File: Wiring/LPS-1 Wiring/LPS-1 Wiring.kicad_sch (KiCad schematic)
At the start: 9 parts, among them J1 Block_Connector_04_b, J2 Battery, J3 Solar charging unit, J4 Solar Panel, J5 LPS-1 Monitoring Unit, J6 Fuse Block, J7 Block_Connector_04_b, SW1 Battery Kill Switch, SW2 Load Monitoring Control

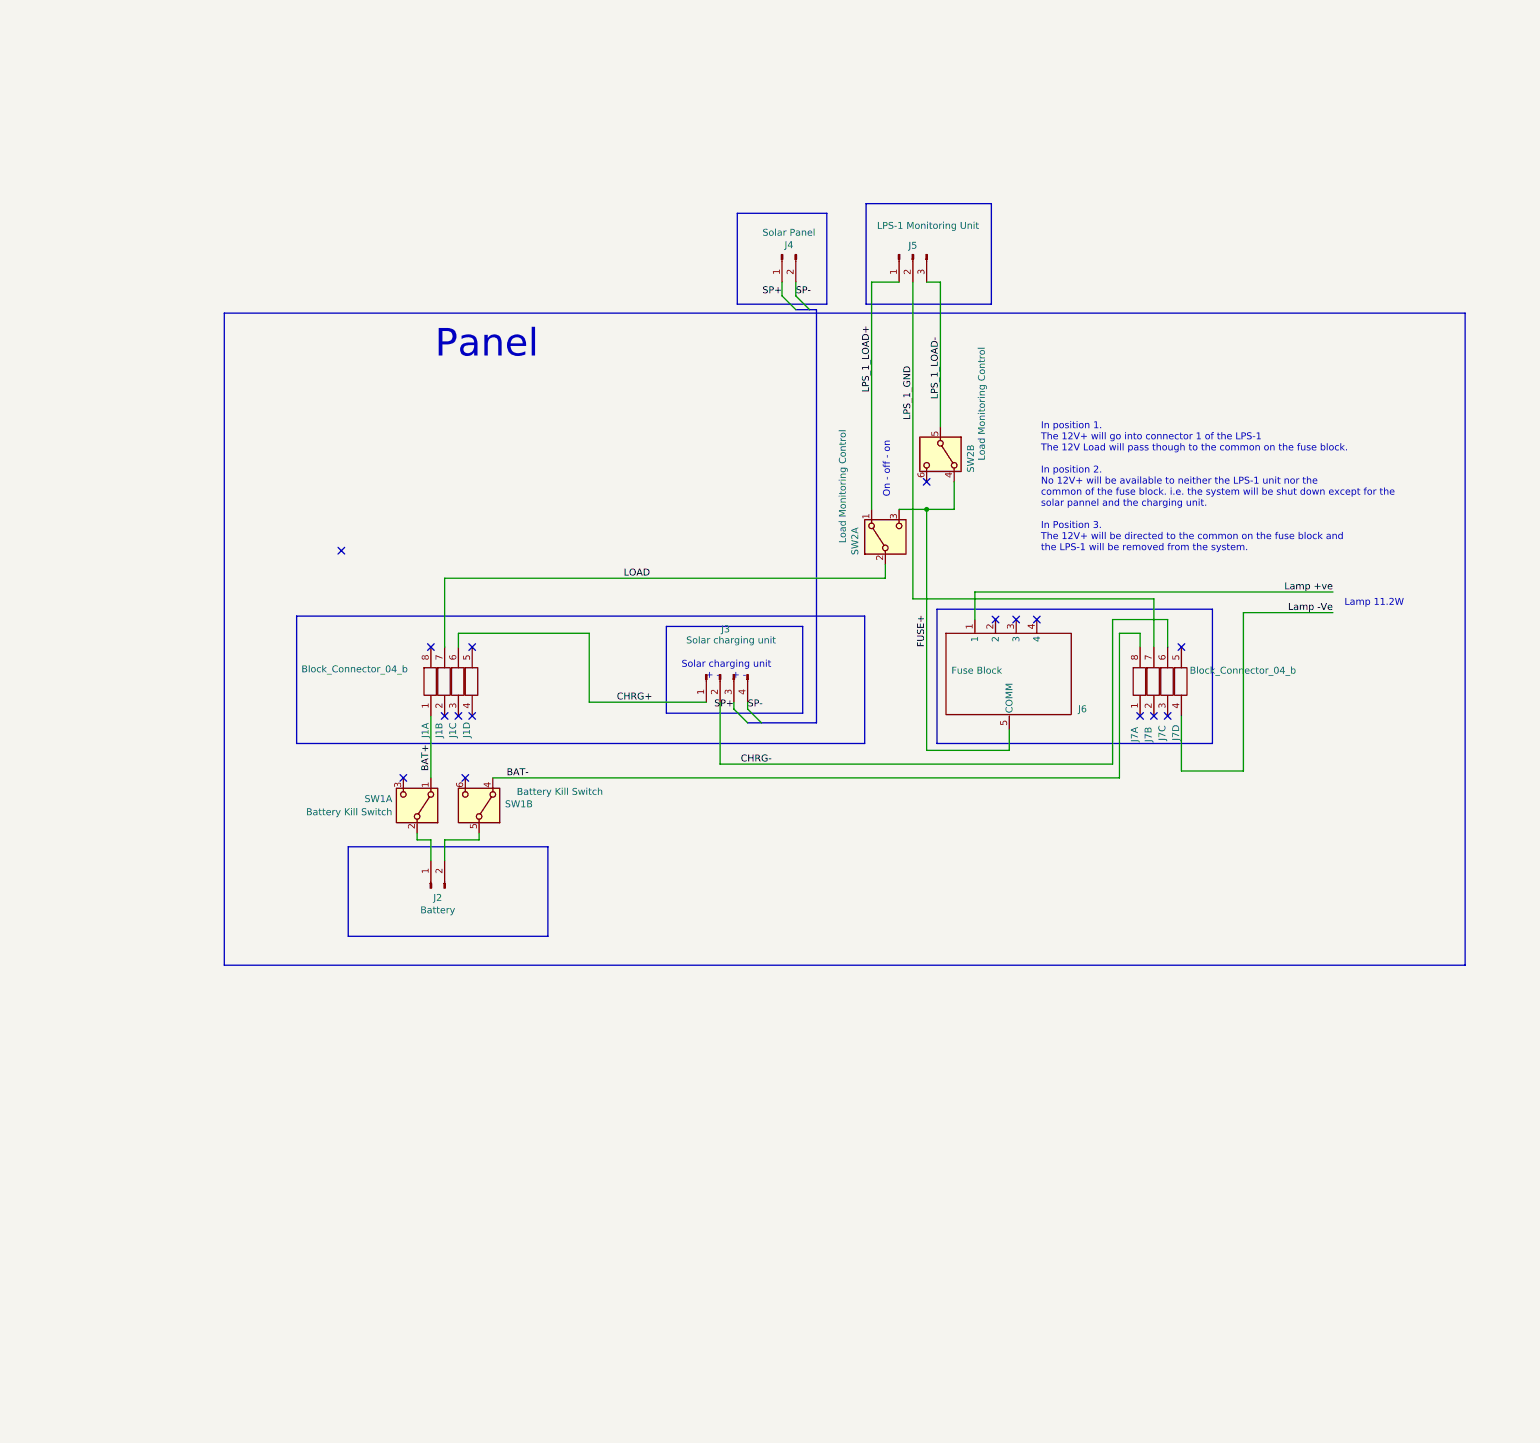
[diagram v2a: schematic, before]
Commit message: Updated the wiring diagram
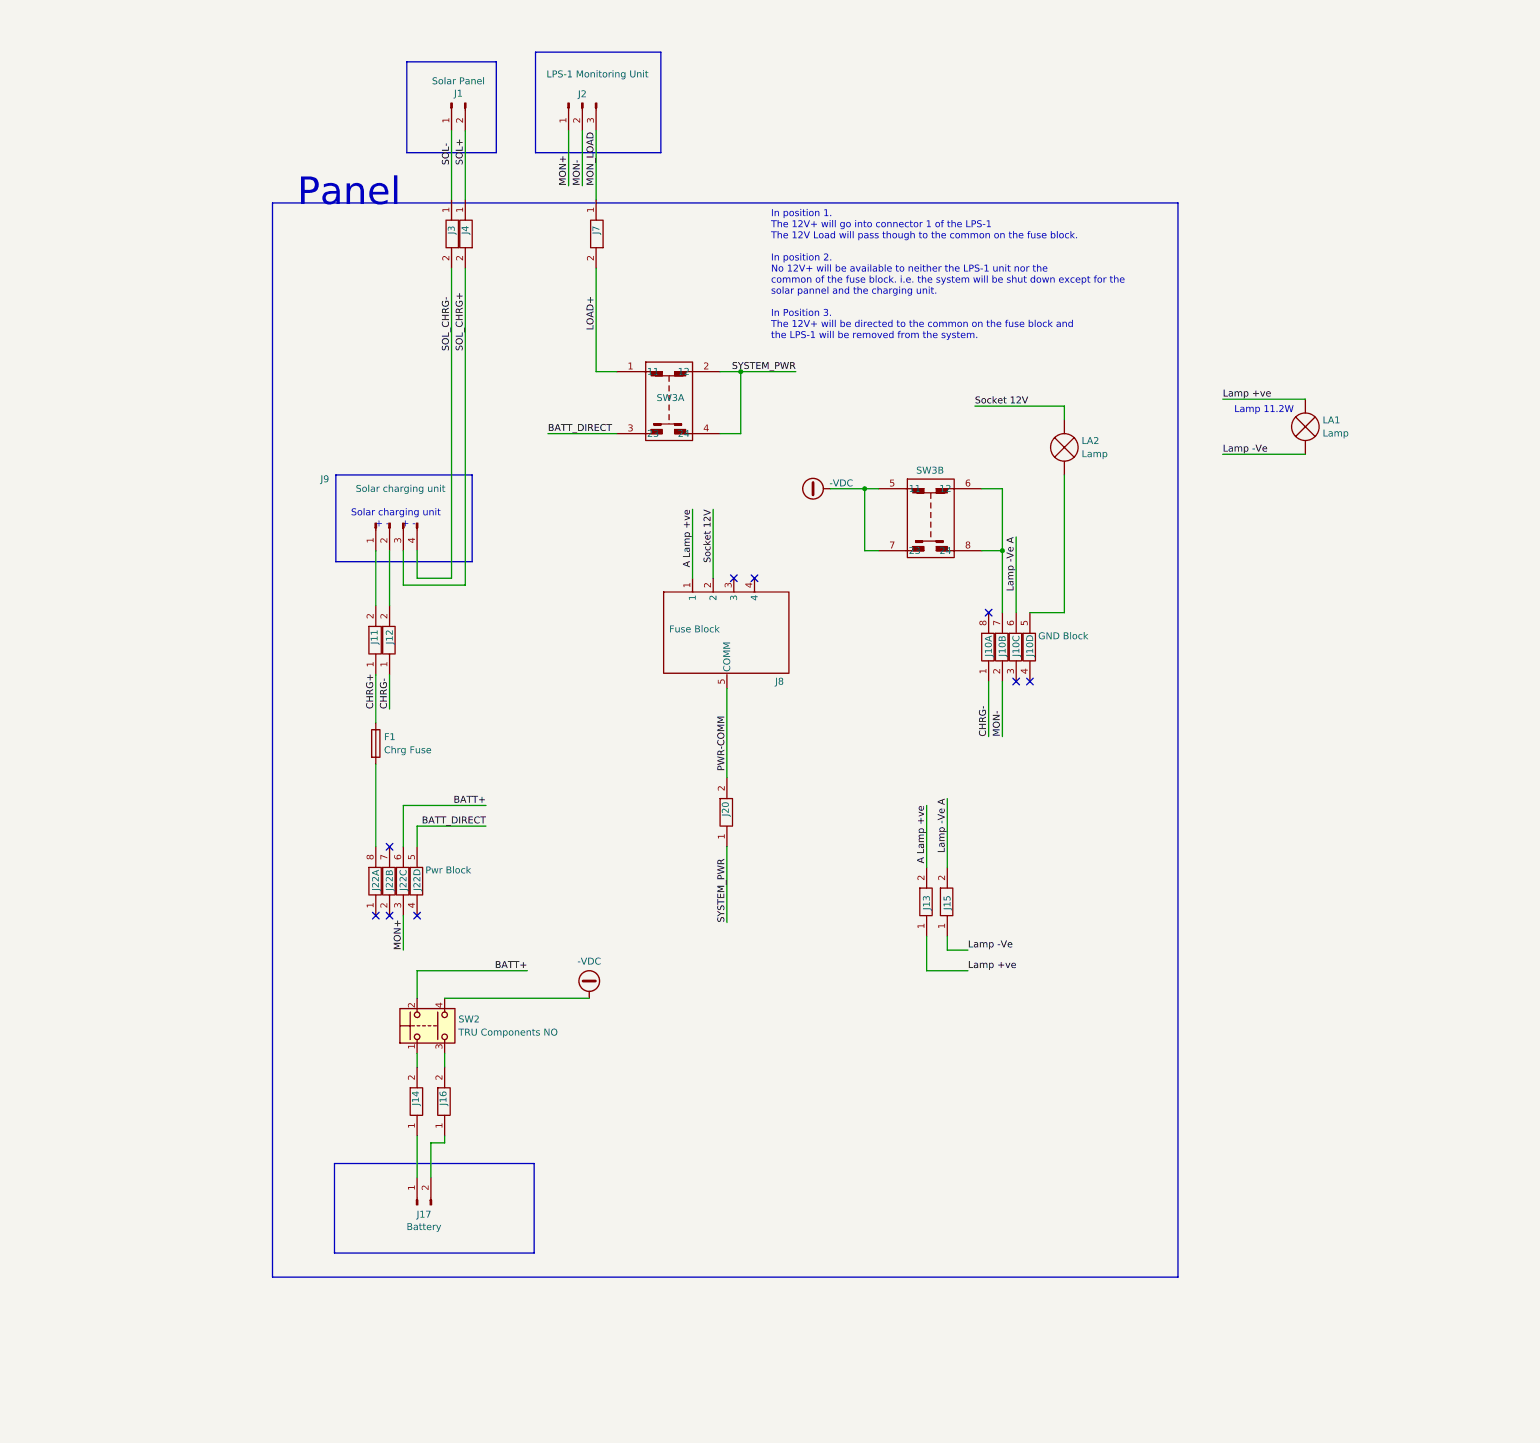
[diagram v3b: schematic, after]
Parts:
- removed J1: Block_Connector_04_b, Wiring:Degson_04_Bridged-PC2.5-01P-11-00AH-1_5.2, symbol Wiring:Block_Connector_04_Pin_B
- removed SW1: Battery Kill Switch, Wiring:SW_101_TC-R13-244D-02, symbol Switch:SW_DPDT_x2
- removed SW2: Load Monitoring Control, Wiring:SW_101_TC-R13-244D-02, symbol Switch:SW_DPDT_x2
- added F1: Chrg Fuse, Connector_PinHeader_2.54mm:PinHeader_1x02_P2.54mm_Vertical, symbol Device:Fuse
- added J11, J12, J13, J14, J15, J16, J20, J3, J4, J7: Block_Connector_01_b, Wiring:Degson_01_PC2.5-01P-11-00AH-1_5.2, symbol Wiring:Block_Connector_01_Pin
- added J22: Pwr Block, Wiring:Degson_04_Bridged-PC2.5-01P-11-00AH-1_5.2, symbol Wiring:Block_Connector_04_Pin_B
- added LA1, LA2: Lamp, Connector_PinHeader_2.54mm:PinHeader_1x02_P2.54mm_Vertical, symbol Device:Lamp
- added SW2: TRU Components NO, Wiring:TruComponents_SW_LAS0_1, symbol Wiring:SW_Push_Dual TRU Components
- added SW3: (no value), Wiring:TruComponents_SW_LAS0, symbol Wiring:TruComponents_Rotary_Switch_LAS0_x2
- J10: renamed from J7; value Block_Connector_04_b -> GND Block
- renumbered J4 to J1, J2 to J17, J5 to J2, J6 to J8, J3 to J9
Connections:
- net CHRG+: now also F1.1, J11.1; no longer J9.1 (Pin_1)
- net CHRG-: now also J10.1, J12.1; no longer J10.6, J9.2 (Pin_2)
- net Lamp +ve: now also J13.1, LA1.2 (+); no longer J8.1
- net Lamp -Ve: now also J15.1, LA1.1 (-); no longer J10.4
- net at J17.1 (Pin_1): now also J14.1
- net at J10.5: now also LA2.1 (-)
- net at J17.2 (Pin_2): now also J16.1
- net Socket 12V: now reaches J8.2
- net Socket 12V: now also LA2.2 (+)
- net MON-: now reaches J10.2
- net MON-: now also J2.2 (Pin_2)
- net BAT-: no longer names the net of J10.8
- net FUSE+ renamed PWR-COMM
- net PWR-COMM: now also J20.2
- net LPS_1_GND: no longer names the net of J10.7
- net LPS_1_GND: now also SW3.6 (12), SW3.8 (24); no longer J2.2 (Pin_2)
- net LPS_1_LOAD+ renamed MON+
- net MON+: now also J22.3
- net LPS_1_LOAD- renamed MON_LOAD
- net MON_LOAD: now also J7.1
- net SP+ renamed SOL-
- net SOL-: now also J3.1; no longer J9.3 (Pin_3)
- net SP- renamed SOL+
- net SOL+: now also J4.1; no longer J9.4 (Pin_4)
- new net: J14.2, SW2.1 (11)
- new net: J16.2, SW2.3 (23)
- new net: J11.2, J9.1 (Pin_1)
- new net: J12.2, J9.2 (Pin_2)
- new net: F1.2, J22.8
- new net -VDC: SW2.4 (24), SW3.5 (11), SW3.7 (23)
- new net A Lamp +ve: J13.2, J8.1
- new net BATT+: J22.6, SW2.2 (12)
- new net BATT_DIRECT: J22.5, SW3.3 (23)
- new net LOAD+: J7.2, SW3.1 (11)
- new net Lamp -Ve A: J10.6, J15.2
- new net SOL_CHRG+: J4.2, J9.3 (Pin_3)
- new net SOL_CHRG-: J3.2, J9.4 (Pin_4)
- new net SYSTEM_PWR: J20.1, SW3.2 (12), SW3.4 (24)
- no-connect marks 16 -> 9
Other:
- note removed: "On - off - on"
- moved on the sheet: J1, J10A, J10B, J10C, J10D, J17, J2, J8, J9

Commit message: Refactored the reference numbering
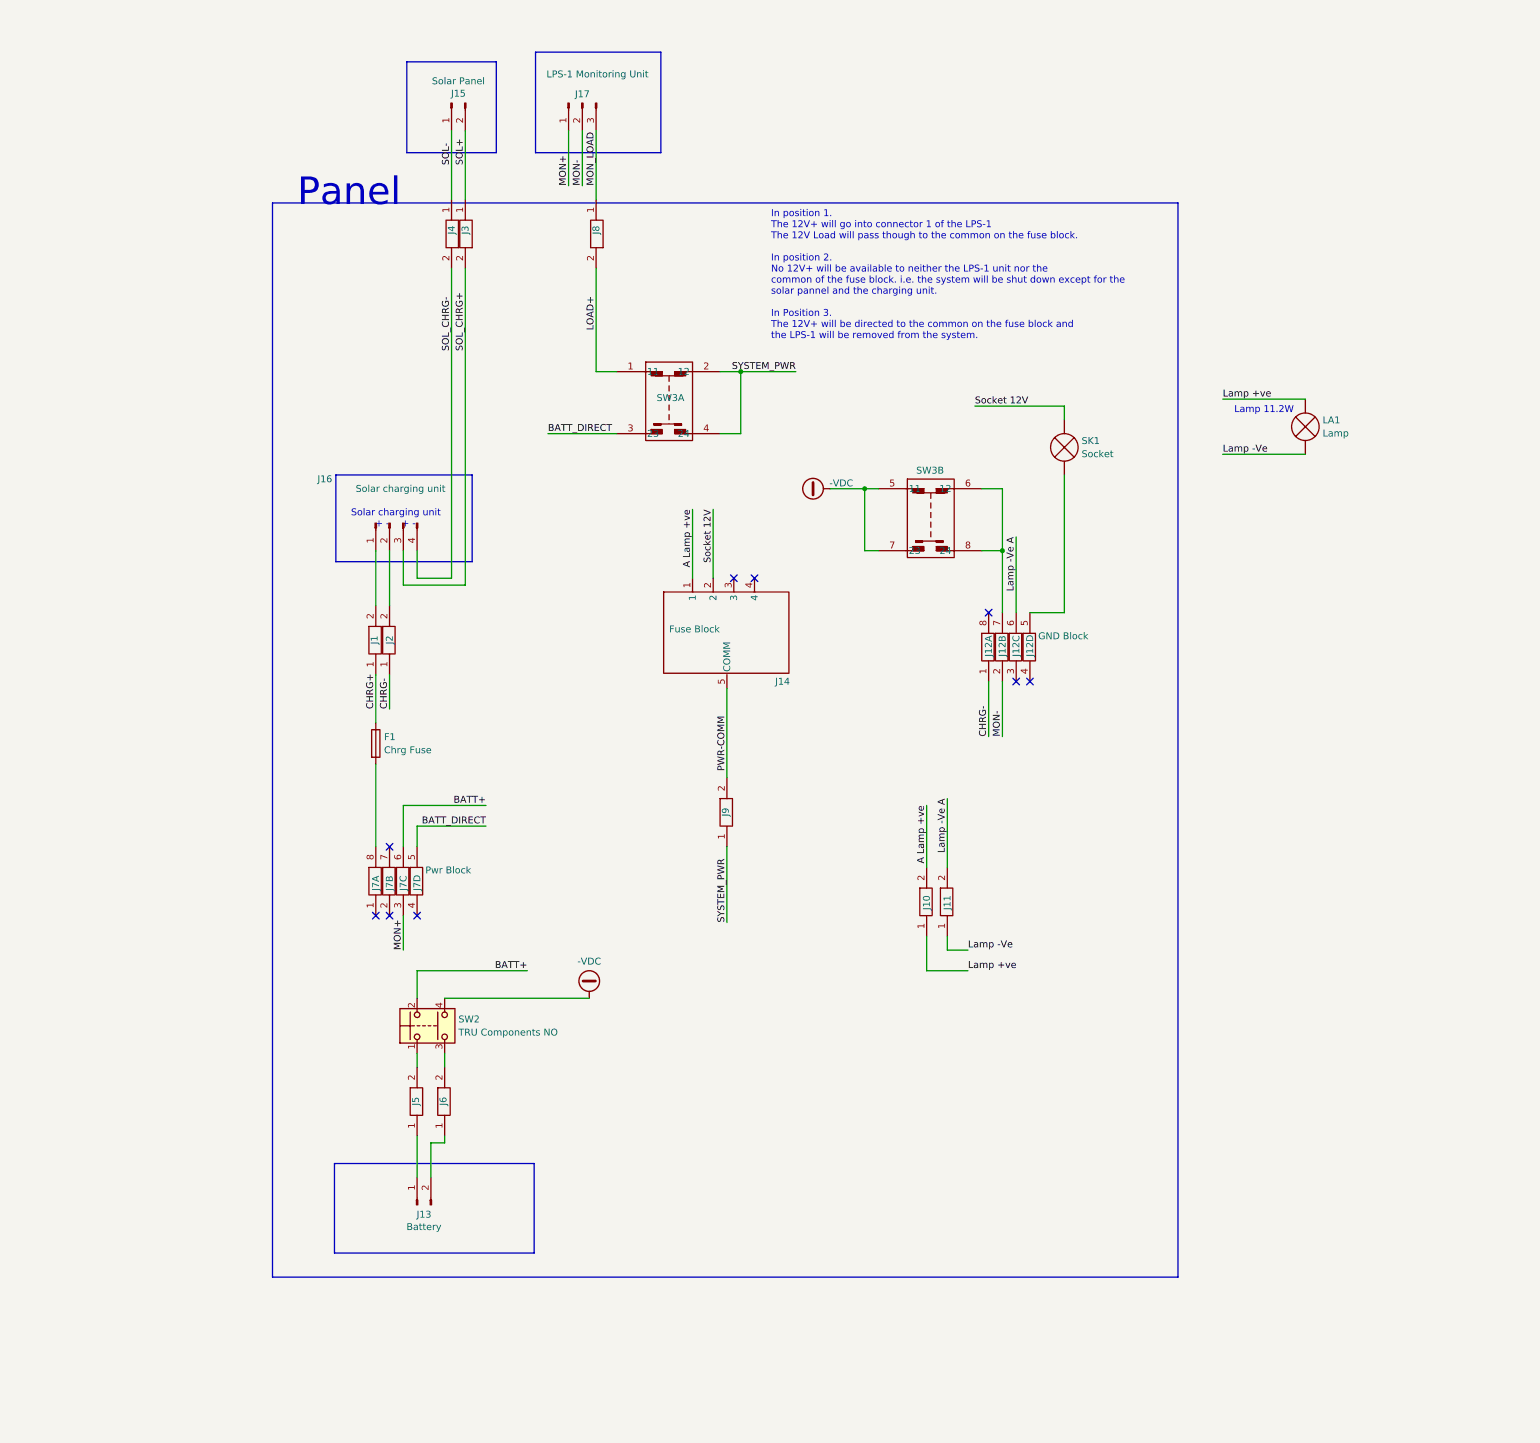
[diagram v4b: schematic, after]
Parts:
- SK1: renamed from LA2; value Lamp -> Socket
- renumbered J11 to J1, J13 to J10, J15 to J11, J10 to J12, J17 to J13, J8 to J14, J1 to J15, J9 to J16, J2 to J17, J12 to J2, J4 to J3, J3 to J4, J14 to J5, J16 to J6, J22 to J7, J7 to J8, J20 to J9
